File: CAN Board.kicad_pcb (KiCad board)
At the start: 4 copper layers, 35 x 50 mm, 97 parts, among them J1 Conn_02x07_Odd_Even, J3 USB_C_Receptacle_USB2.0_16P, J4 Conn_01x02, J5 Conn_01x02, J6 Conn_01x02, J7 Conn_01x02, J8 Conn_01x02, J9 Conn_01x02, SW1 SW_Push, SW2 SW_Push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

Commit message: moving stuff
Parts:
- moved R6 8.49 mm to (32.5, 25.5), turned to 180 degrees
- moved C22 1.50 mm to (57.0, 16.5)
- moved C23 1.50 mm to (57.0, 14.5)
- moved C29 1.50 mm to (57.0, 25.0)
- moved C30 1.50 mm to (57.0, 23.0)
- moved C36 1.50 mm to (57.0, 33.5)
- moved C37 1.50 mm to (57.0, 31.5)
- moved C43 1.50 mm to (57.0, 42.5)
- moved C44 1.50 mm to (57.0, 40.5)
- moved R10 1.50 mm to (57.0, 21.5)
- moved R11 1.50 mm to (57.0, 35.0)
- moved R12 1.50 mm to (57.0, 30.0)
- moved R13 1.50 mm to (57.0, 44.0)
- moved R14 1.50 mm to (57.0, 39.0)
- moved R7 1.50 mm to (57.0, 18.0)
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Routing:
- net /QSPI_SS: track 15.4 -> 3.08 mm, vias 0 -> 2
- net GND: track 147.3 -> 136.0 mm, vias 13 -> 11
- net CAN5L: track 7.14 -> 0.00 mm
- net CAN5H: track 7.02 -> 0.00 mm
- net CAN6H: track 6.77 -> 0.00 mm
- net +3V3: track 102.8 -> 106.1 mm
- net Net-(R5-Pad2): track 0.00 -> 3.14 mm
- net CAN2H: track 8.52 -> 11.3 mm
- net CAN3H: track 7.98 -> 10.7 mm
- net CAN1H: track 9.06 -> 11.8 mm
- net CAN4H: track 7.27 -> 9.86 mm
- net CAN4L: track 6.89 -> 9.19 mm
- net CAN3L: track 7.06 -> 8.48 mm
- net CAN2L: track 7.22 -> 8.24 mm

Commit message: moving components
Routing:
- net Net-(C51-Pad1): track 1.52 -> 0.07 mm
- net Net-(C50-Pad1): track 1.52 -> 0.07 mm
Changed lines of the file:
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@@
-	)
-	(segment
-		(start 57.825 51)
-		(end 57.825 52.45)
-		(width 0.1524)
-		(layer "F.Cu")
-		(net 18)
 	)
 	(segment
@@
 	)
 	(segment
-		(start 57.825 49)
-		(end 57.825 47.55)
-		(width 0.1524)
-		(layer "F.Cu")
-		(net 19)
-	)
-	(segment

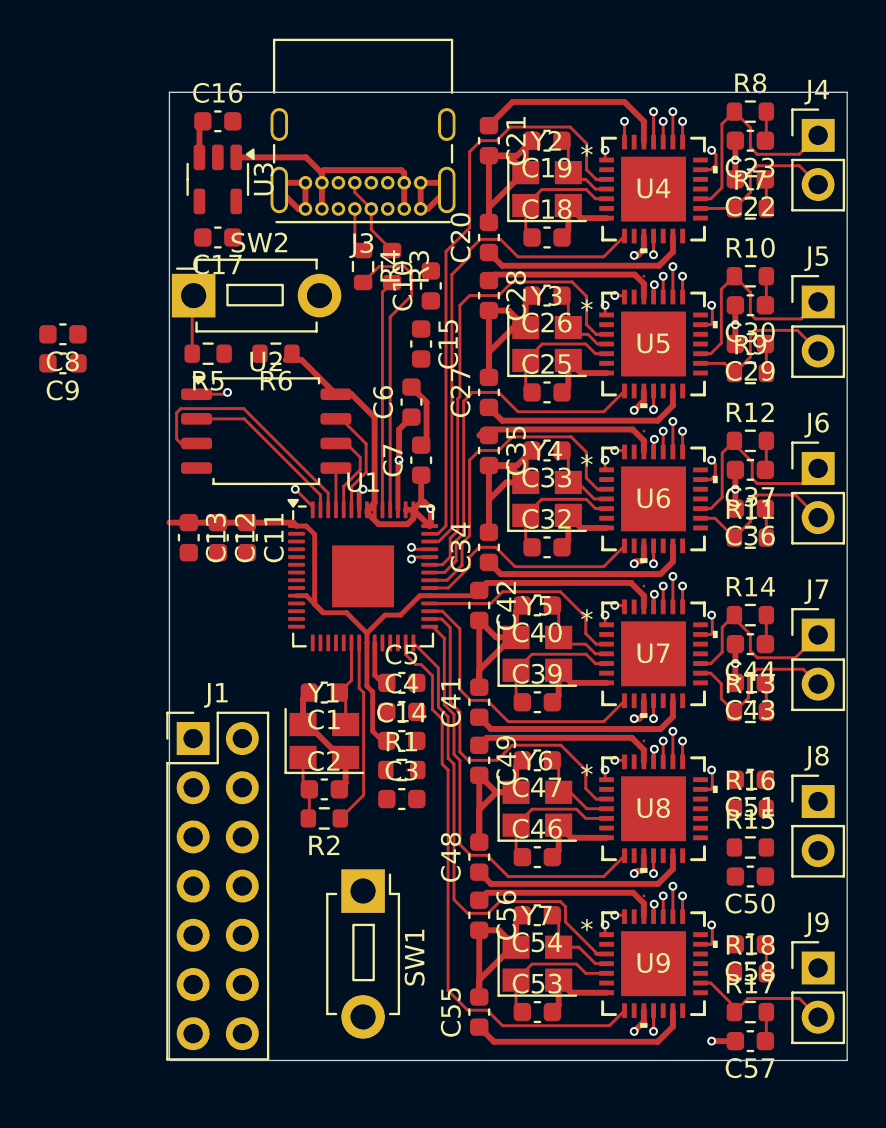
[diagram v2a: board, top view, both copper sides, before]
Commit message: routed data, power lift
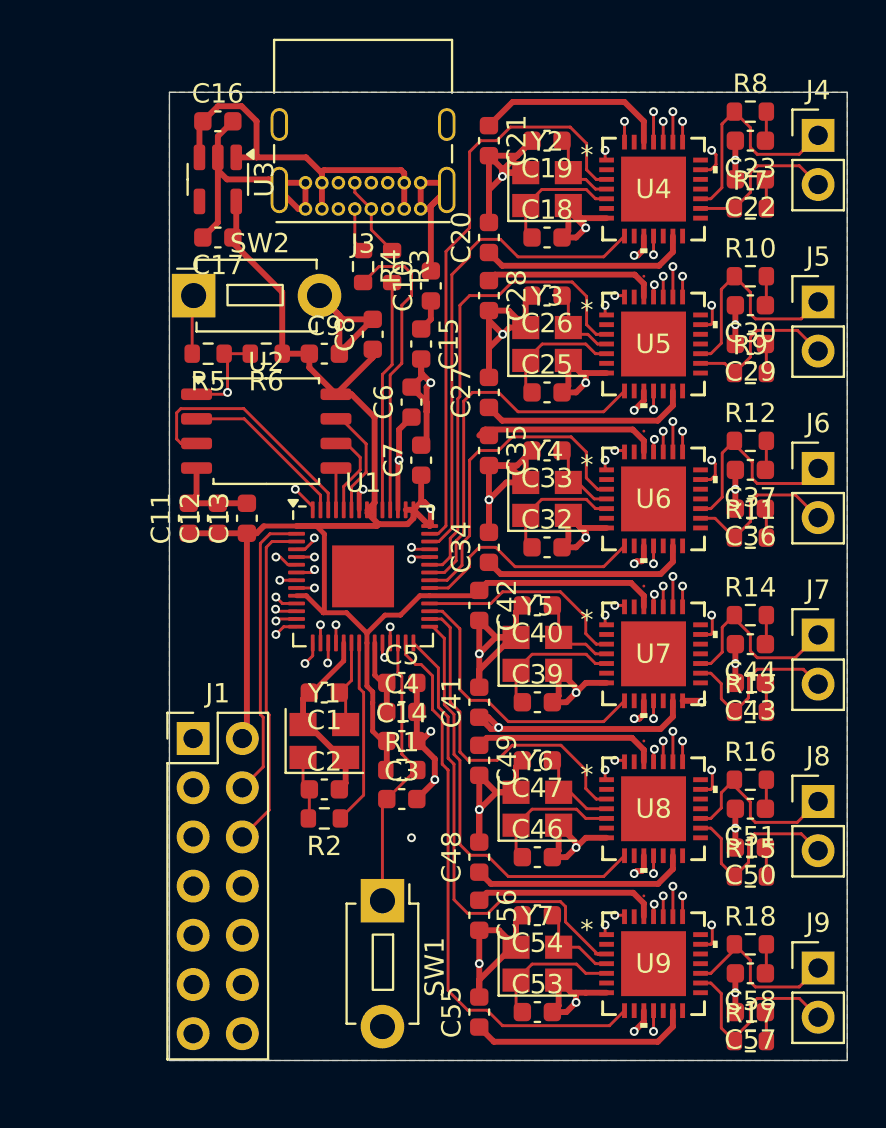
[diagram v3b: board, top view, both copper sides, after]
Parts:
- moved C8 16.0 mm to (37.5, 24.5), turned to 90 degrees
- moved C9 13.5 mm to (35.0, 25.5), turned to 0 degrees
- moved C11 3.16 mm to (28.0, 34.0), turned to 90 degrees
- moved C13 3.16 mm to (31.0, 34.0), turned to 90 degrees
- moved C50 1.50 mm to (57.0, 51.0)
- moved C51 1.50 mm to (57.0, 49.0)
- moved C57 1.50 mm to (57.0, 59.5)
- moved C58 1.50 mm to (57.0, 57.5)
- moved R15 1.50 mm to (57.0, 52.5)
- moved R16 1.50 mm to (57.0, 47.5)
- moved R17 1.50 mm to (57.0, 61.0)
- moved R18 1.50 mm to (57.0, 56.0)
- moved SW1 1.12 mm to (38.0, 53.8)
- moved C12 1.00 mm to (29.5, 34.0), turned to 90 degrees
- moved R6 0.50 mm to (32.0, 25.5)
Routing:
- net GND: track 136.0 -> 202.9 mm, vias 11 -> 27
- net SPI0 1CS: track 1.57 -> 34.4 mm, vias 1 -> 2
- net +3V3: track 106.1 -> 137.9 mm, vias 1 -> 2
- net SPI0 2CS: track 0.66 -> 31.5 mm, vias 1 -> 2
- net SPI0 6CS: track 0.66 -> 28.3 mm, vias 1 -> 2
- net GPIO 15: track 0.00 -> 26.6 mm, vias 0 -> 1
- net SWD: track 0.00 -> 25.1 mm, vias 0 -> 1
- net ADC 1: track 0.98 -> 25.4 mm
- net ADC 0: track 1.04 -> 25.2 mm, vias 1 -> 2
- net SPI0 RX: track 46.4 -> 70.2 mm, vias 6 -> 7
- net SPI0 5CS: track 0.67 -> 24.3 mm, vias 1 -> 2
- net SPI0 SCK: track 46.4 -> 70.0 mm, vias 6 -> 7
- net SPI1 CSn: track 0.00 -> 22.0 mm, vias 0 -> 1
- net SPI1 SCK: track 0.00 -> 22.0 mm, vias 0 -> 1
- net SPI0 3CS: track 0.67 -> 22.3 mm, vias 1 -> 2
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- added copper zone on B.Cu, net GND

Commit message: it has no errors :)
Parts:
- added J10: Conn_01x03, Connector_Molex:Molex_PicoBlade_53047-0310_1x03_P1.25mm_Vertical, F.Cu at (28.6, 38.8)
- added J11: Conn_01x03, Connector_Molex:Molex_PicoBlade_53047-0310_1x03_P1.25mm_Vertical, F.Cu at (28.6, 46.2)
- added J2: Conn_01x06, Connector_Molex:Molex_PicoBlade_53047-0610_1x06_P1.25mm_Vertical, F.Cu at (28.6, 53.9)
- J1: value Conn_02x07_Odd_Even -> Conn_01x04; footprint Connector_PinHeader_2.54mm:PinHeader_2x07_P2.54mm_Vertical -> Connector_Molex:Molex_PicoBlade_53047-0410_1x04_P1.25mm_Vertical
- J3: footprint Connector_USB:USB_C_Receptacle_GCT_USB4085 -> Connector_USB:USB_C_Receptacle_G-Switch_GT-USB-7010ASV
- moved J1 10.9 mm to (33.0, 55.1), turned to -90 degrees
- moved J3 4.61 mm to (37.0, 14.5)
- moved R3 1.50 mm to (37.0, 21.0)
- moved R4 1.50 mm to (38.5, 21.0)
- moved SW1 0.50 mm to (38.5, 53.8)
- moved U2 0.25 mm to (32.2, 29.5)
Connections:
- J1 pad 1: +5V -> GND
- J1 pad 2: +3V3 -> ADC 0
- J1 pad 3: GND -> ADC 1
- J1 pad 4: TX0 -> GPIO 15
- R3 pad 2: /ucd- -> /ucd+
- R4 pad 2: /ucd+ -> /ucd-
- U1 pad 46: /ucd+ -> /ucd-
- U1 pad 47: /ucd- -> /ucd+
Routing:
- net +5V: track 88.5 -> 55.7 mm, vias 1 -> 15
- net +1V1: track 9.95 -> 25.4 mm
- net RX0: track 17.3 -> 8.87 mm
- net TX0: track 15.2 -> 8.26 mm
- net SWD: track 25.1 -> 18.9 mm
- net SWCLK: track 20.7 -> 15.0 mm
- net +3V3: track 137.9 -> 132.2 mm, vias 2 -> 18
- net SPI0 3CS: track 22.3 -> 28.0 mm
- net SPI1 TX: track 13.5 -> 18.9 mm
- net SPI0 2CS: track 31.5 -> 27.6 mm
- net GND: track 202.9 -> 206.6 mm, vias 27 -> 32
- net GPIO 15: track 26.6 -> 23.0 mm
- net SPI0 5CS: track 24.3 -> 27.5 mm
- net /ucd+: track 15.6 -> 12.6 mm
- net SPI0 6CS: track 28.3 -> 31.1 mm
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- added copper zone on In2.Cu, net +3V3
- added copper zone on In1.Cu, net +5V

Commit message: cleaning up and minor updates
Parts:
- J3: footprint Connector_USB:USB_C_Receptacle_G-Switch_GT-USB-7010ASV -> Connector_USB:USB_C_Receptacle_GCT_USB4105-xx-A_16P_TopMnt_Horizontal
- moved J1 0.71 mm to (33.5, 54.6)
- moved J10 0.71 mm to (29.1, 38.2)
- moved J11 0.71 mm to (29.1, 45.8)
- moved J2 0.71 mm to (29.1, 53.4)
- moved SW1 0.71 mm to (39.0, 53.2)
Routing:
- net GND: track 206.6 -> 209.4 mm, vias 32 -> 31
- net ADC 0: track 23.9 -> 23.2 mm
- net TX0: track 8.26 -> 7.55 mm
- net RX0: track 8.87 -> 8.16 mm
- net SWCLK: track 15.0 -> 14.3 mm
- net SPI1 TX: track 18.9 -> 18.1 mm
- net SPI1 RX: track 19.8 -> 19.1 mm
- net SPI1 CSn: track 21.0 -> 20.3 mm
- net ADC 1: track 26.6 -> 25.9 mm
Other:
- board text added: "BOOT"
- board text added: "GPIO"
- board text added: "RST"
- board text added: "SPI"
- board text added: "SWD"
- board text added: "UART"

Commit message: slight moving of parts
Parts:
- moved J1 0.50 mm to (34.0, 54.6)
- moved SW1 0.50 mm to (39.5, 53.2)
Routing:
- net RUN: track 14.5 -> 15.4 mm
- net ADC 0: track 23.2 -> 23.8 mm
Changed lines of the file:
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@@
 	(footprint "Connector_Molex:Molex_PicoBlade_53047-0410_1x04_P1.25mm_Vertical"
 		(layer "F.Cu")
-		(at 33.55 54.625 -90)
+		(at 34.05 54.625 -90)
 		(descr "Molex PicoBlade Connector System, 53047-0410, 4 Pins per row (http://www.molex.com/pdm_docs/sd/530470610_sd.pdf), generated with kicad-footprint-generator")
 		(tags "connector Molex PicoBlade side entry")
@@
 	(footprint "Button_Switch_THT:SW_PUSH_1P1T_6x3.5mm_H5.0_APEM_MJTP1250"
 		(layer "F.Cu")
-		(at 39 53.25 -90)
+		(at 39.5 53.25 -90)
 		(descr "tactile push button, 6x3.5mm, https://www.apem.com/idec-apem/en_US/PCB-switches/Tactile-Switches/MJTP-6mm-through-hole/c/MJTP_6mm_through%20hole?page=1")
 		(tags "PHAP3362A 6mm tact sw THT")
@@
 	)
 	(segment
+		(start 39.5 52.75)
+		(end 39 53.25)
+		(width 0.1524)
+		(layer "F.Cu")
+		(net 4)
+	)
+	(segment
 		(start 39.825 47)
 		(end 39.725 47)
@@
 	)
 	(segment
-		(start 38.8 41.032631)
-		(end 39 41.232631)
+		(start 38.225 48.5)
+		(end 38.225 48.725)
 		(width 0.1524)
 		(layer "F.Cu")
@@
 	)
 	(segment
-		(start 38 48.5)
-		(end 38 48.3)
+		(start 39.5 50)
+		(end 39.5 53.25)
 		(width 0.1524)
 		(layer "F.Cu")
@@
 	)
 	(segment
-		(start 38.8 40.4375)
-		(end 38.8 41.032631)
+		(start 38.8 41.032631)
+		(end 39 41.232631)
 		(width 0.1524)
 		(layer "F.Cu")
@@
 	)
 	(segment
-		(start 39 41.232631)
-		(end 39 46.175)
+		(start 38 48.5)
+		(end 38 48.3)
 		(width 0.1524)
 		(layer "F.Cu")
@@
 	)
 	(segment
-		(start 39 49.275)
-		(end 39 53.25)
+		(start 38.225 48.725)
+		(end 39.5 50)
 		(width 0.1524)
 		(layer "F.Cu")
@@
 	)
 	(segment
-		(start 38.225 48.5)
-		(end 39 49.275)
+		(start 38.8 40.4375)
+		(end 38.8 41.032631)
+		(width 0.1524)
+		(layer "F.Cu")
+		(net 4)
+	)
+	(segment
+		(start 39 41.232631)
+		(end 39 46.175)
 		(width 0.1524)
 		(layer "F.Cu")
@@
 	)
 	(segment
-		(start 36.7413 54.2587)
-		(end 33.875 57.125)
+		(start 39.5 35.5)
+		(end 40.0332 36.0332)
 		(width 0.1524)
 		(layer "In2.Cu")
@@
 	)
 	(segment
-		(start 39.5 37.0332)
-		(end 39.720859 37.0332)
+		(start 34.875 57.125)
+		(end 34.05 57.125)
 		(width 0.1524)
 		(layer "In2.Cu")
@@
 	)
 	(segment
-		(start 40.0332 36.0332)
-		(end 39.5 35.5)
+		(start 37.4668 39.0664)
+		(end 37.4668 40.123277)
 		(width 0.1524)
 		(layer "In2.Cu")
@@
 	)
 	(segment
-		(start 37.4668 39.0664)
-		(end 39.5 37.0332)
+		(start 39.5 37.0332)
+		(end 37.4668 39.0664)
 		(width 0.1524)
 		(layer "In2.Cu")
@@
 	(segment
 		(start 36.7413 40.848777)
-		(end 37.4668 40.123277)
+		(end 36.7413 55.2587)
 		(width 0.1524)
 		(layer "In2.Cu")
@@
 	(segment
 		(start 40.0332 36.720859)
-		(end 40.0332 36.0332)
+		(end 39.720859 37.0332)
 		(width 0.1524)
 		(layer "In2.Cu")
@@
 	)
 	(segment
-		(start 33.875 57.125)
-		(end 33.55 57.125)
+		(start 39.720859 37.0332)
+		(end 39.5 37.0332)
 		(width 0.1524)
 		(layer "In2.Cu")
@@
 	)
 	(segment
-		(start 39.5 35.5)
-		(end 39.463024 35.5)
+		(start 37.4668 40.123277)
+		(end 36.7413 40.848777)
 		(width 0.1524)
 		(layer "In2.Cu")
@@
 	)
 	(segment
-		(start 36.7413 54.2587)
-		(end 36.7413 40.848777)
+		(start 39.5 35.5)
+		(end 39.463024 35.5)
 		(width 0.1524)
 		(layer "In2.Cu")
@@
 	)
 	(segment
-		(start 39.720859 37.0332)
+		(start 40.0332 36.0332)
 		(end 40.0332 36.720859)
 		(width 0.1524)
@@
 	)
 	(segment
-		(start 37.4668 40.123277)
-		(end 37.4668 39.0664)
+		(start 36.7413 55.2587)
+		(end 34.875 57.125)
 		(width 0.1524)
 		(layer "In2.Cu")
@@
 	)
 	(segment
+		(start 36.998892 39.001108)
+		(end 36.998892 39.840011)
+		(width 0.1524)
+		(layer "In2.Cu")
+		(net 150)
+	)
+	(segment
 		(start 33.8524 55.875)
 		(end 33.55 55.875)
@@
 	)
 	(segment
-		(start 39.5 36.5)
-		(end 36.998892 39.001108)
+		(start 36.998892 39.840011)
+		(end 36.5 40.338903)
 		(width 0.1524)
 		(layer "In2.Cu")
@@
 	)
 	(segment
-		(start 36.998892 39.001108)
-		(end 36.998892 39.840011)
+		(start 36.5 40.338903)
+		(end 36.5 54.5)
 		(width 0.1524)
 		(layer "In2.Cu")
@@
 	)
 	(segment
-		(start 36.998892 39.840011)
-		(end 36.5 40.338903)
+		(start 35.125 55.875)
+		(end 34.05 55.875)
 		(width 0.1524)
 		(layer "In2.Cu")
@@
 	)
 	(segment
-		(start 36.5 53.2274)
-		(end 33.8524 55.875)
+		(start 39.5 36.5)
+		(end 36.998892 39.001108)
 		(width 0.1524)
 		(layer "In2.Cu")
@@
 	)
 	(segment
-		(start 36.5 40.338903)
-		(end 36.5 53.2274)
+		(start 36.5 54.5)
+		(end 35.125 55.875)
 		(width 0.1524)
 		(layer "In2.Cu")

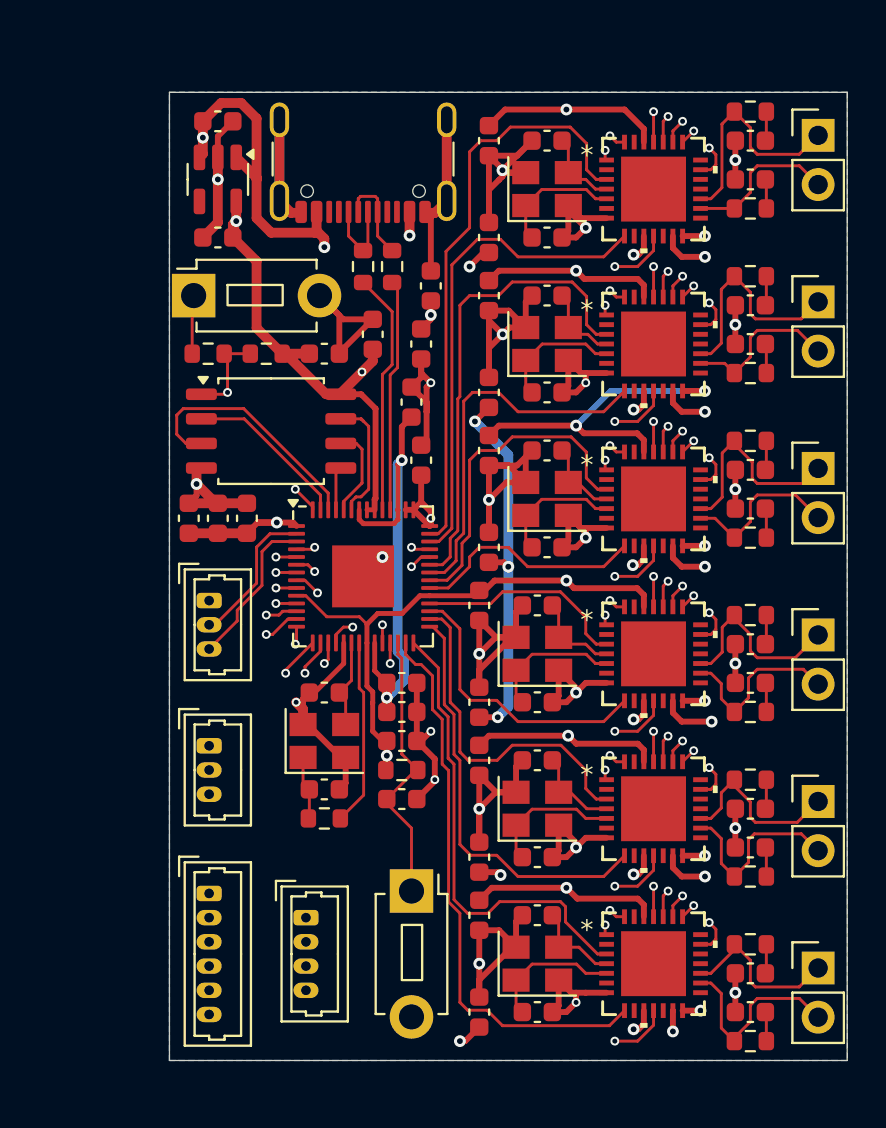
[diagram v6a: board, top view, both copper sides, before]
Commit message: added mounting holes
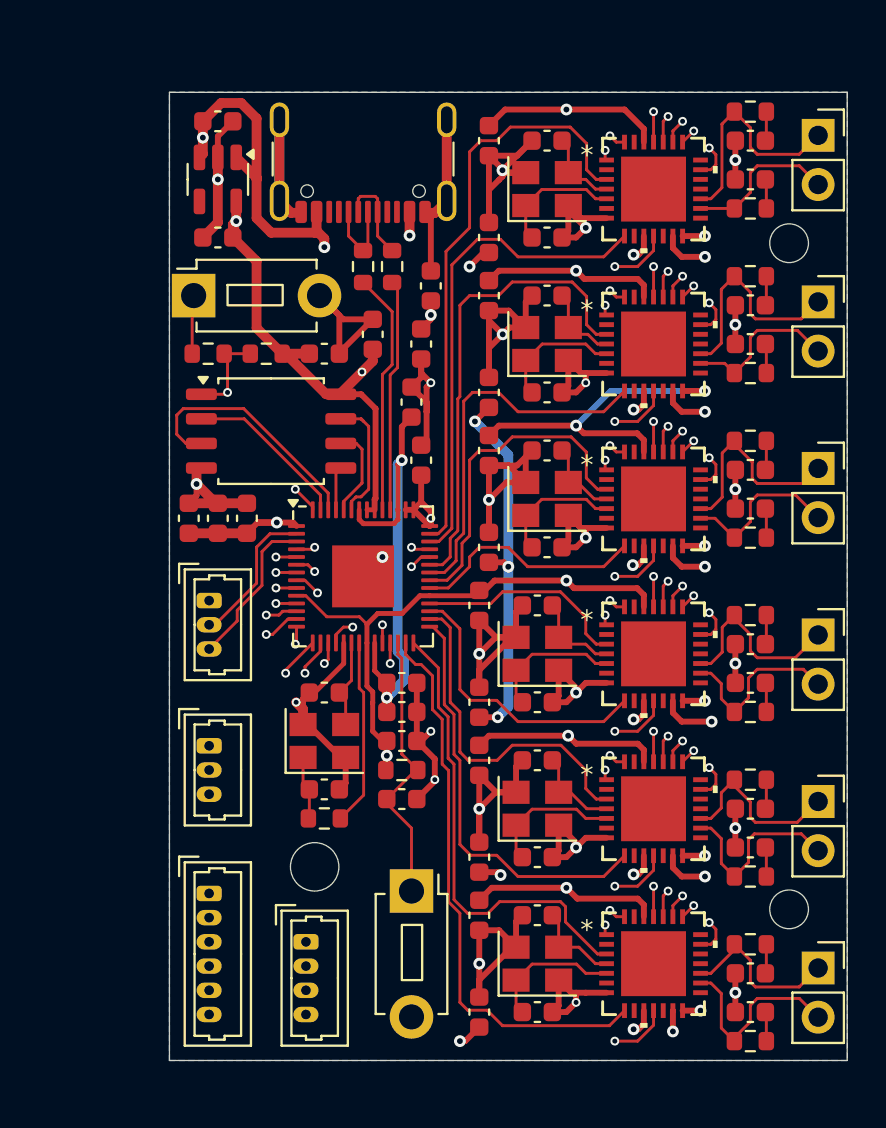
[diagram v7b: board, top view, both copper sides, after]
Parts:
- J4, J5, J6, J7, J8, J9: footprint Connector_PinHeader_2.54mm:PinHeader_1x02_P2.54mm_Vertical -> Connector_PinSocket_2.54mm:PinSocket_1x02_P2.54mm_Vertical
- moved J1 1.25 mm to (34.0, 55.9)
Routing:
- net GPIO 15: track 23.4 -> 24.6 mm
- net ADC 1: track 26.0 -> 27.1 mm
- net ADC 0: track 23.8 -> 24.4 mm
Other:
- outline, holes or cut-outs redrawn
